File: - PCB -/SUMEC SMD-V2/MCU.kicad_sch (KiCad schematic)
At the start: 29 parts, among them IC2 DRV8874PWPR, IC3 DRV8874PWPR, J5 TYPE-C-31-M-12, SW2 SW_Push, SW3 SW_Push, U2 ESP32-S3-WROOM-1, U3 USBLC6-2SC6

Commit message: final fuckup cleanup
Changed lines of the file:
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@@
   )
   (text "0.1-µF bypass capacitor to ground, as well as\nsufficient Bulk Capacitance rated for VM"
-    (at 66.04 317.5 0)
+    (at 77.47 363.22 0)
     (effects (font (face "Bahnschrift") (size 1.27 1.27)) (justify left bottom))
   )
@@
   )
   (text "Sleep mode input. Logic high to enable device. \nLogic low to enter low-power sleep mode."
-    (at 66.04 312.42 0)
+    (at 77.47 358.14 0)
     (effects (font (face "Bahnschrift") (size 1.27 1.27)) (justify left bottom))
   )
@@
     (effects (font (face "Bahnschrift") (size 1.27 1.27)) (justify left bottom))
   )
-  (text "Overcurrent protection - Current regulation" (at 66.04 322.58 0)
+  (text "Overcurrent protection - Current regulation" (at 77.47 368.3 0)
     (effects (font (face "Bahnschrift") (size 1.27 1.27)) (justify left bottom))
   )
@@
   )
   (text "Analog current output propotaional to load current."
-    (at 66.04 320.04 0)
+    (at 77.47 365.76 0)
     (effects (font (face "Bahnschrift") (size 1.27 1.27)) (justify left bottom))
   )
@@
     (effects (font (face "Bahnschrift") (size 1.27 1.27)) (justify left bottom))
   )
-  (text "H-bridge control input mode." (at 66.04 307.34 0)
+  (text "H-bridge control input mode." (at 77.47 353.06 0)
     (effects (font (face "Bahnschrift") (size 1.27 1.27)) (justify left bottom))
   )
@@
   )
   (text "(nFault)Fault indicator output. Pulled low during a fault condition. \nConnect an external pullup resistor\nfor open-drain operation."
-    (at 66.04 302.26 0)
+    (at 77.47 347.98 0)
     (effects (font (face "Bahnschrift") (size 1.27 1.27)) (justify left bottom))
   )

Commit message: Board and BOM update
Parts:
- C16, C3, C5: footprint Capacitor_Tantalum_SMD:CP_EIA-2012-12_Kemet-R_Pad1.30x1.05mm_HandSolder -> Capacitor_Tantalum_SMD:CP_EIA-3216-18_Kemet-A_Pad1.58x1.35mm_HandSolder
- D3: footprint Diode_SMD:D_0805_2012Metric_Pad1.15x1.40mm_HandSolder -> Diode_SMD:D_1206_3216Metric_Pad1.42x1.75mm_HandSolder
- R4: footprint Resistor_SMD:R_0805_2012Metric_Pad1.20x1.40mm_HandSolder -> Resistor_SMD:R_1206_3216Metric_Pad1.30x1.75mm_HandSolder
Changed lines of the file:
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@@
       (effects (font (face "Bahnschrift") (size 1.27 1.27)))
     )
-    (property "Footprint" "Diode_SMD:D_0805_2012Metric_Pad1.15x1.40mm_HandSolder" (at 416.56 129.54 0)
+    (property "Footprint" "Diode_SMD:D_1206_3216Metric_Pad1.42x1.75mm_HandSolder" (at 416.56 129.54 0)
       (effects (font (face "Bahnschrift") (size 1.27 1.27)) hide)
     )
@@
       (effects (font (face "Bahnschrift") (size 1.27 1.27)))
     )
-    (property "Footprint" "Resistor_SMD:R_0805_2012Metric_Pad1.20x1.40mm_HandSolder" (at 417.83 145.542 90)
+    (property "Footprint" "Resistor_SMD:R_1206_3216Metric_Pad1.30x1.75mm_HandSolder" (at 417.83 145.542 90)
       (effects (font (face "Bahnschrift") (size 1.27 1.27)) hide)
     )
@@
       (effects (font (face "Bahnschrift") (size 1.27 1.27)) (justify left))
     )
-    (property "Footprint" "Capacitor_Tantalum_SMD:CP_EIA-2012-12_Kemet-R_Pad1.30x1.05mm_HandSolder" (at 233.9848 313.69 0)
+    (property "Footprint" "Capacitor_Tantalum_SMD:CP_EIA-3216-18_Kemet-A_Pad1.58x1.35mm_HandSolder" (at 233.9848 313.69 0)
       (effects (font (face "Bahnschrift") (size 1.27 1.27)) hide)
     )
@@
       (effects (font (face "Bahnschrift") (size 1.27 1.27)) (justify left))
     )
-    (property "Footprint" "Capacitor_Tantalum_SMD:CP_EIA-2012-12_Kemet-R_Pad1.30x1.05mm_HandSolder" (at 231.4448 356.87 0)
+    (property "Footprint" "Capacitor_Tantalum_SMD:CP_EIA-3216-18_Kemet-A_Pad1.58x1.35mm_HandSolder" (at 231.4448 356.87 0)
       (effects (font (face "Bahnschrift") (size 1.27 1.27)) hide)
     )
@@
       (effects (font (face "Bahnschrift") (size 1.27 1.27)) (justify left))
     )
-    (property "Footprint" "Capacitor_Tantalum_SMD:CP_EIA-2012-12_Kemet-R_Pad1.30x1.05mm_HandSolder" (at 209.8548 135.89 0)
-      (effects (font (face "Bahnschrift") (size 1.27 1.27)) hide)
-    )
+    (property "Footprint" "Capacitor_Tantalum_SMD:CP_EIA-3216-18_Kemet-A_Pad1.58x1.35mm_HandSolder" (at 209.8548 135.89 0)
+      (effects (font (face "Bahnschrift") (size 1.27 1.27)) hide)
+    )

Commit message: PCB Inspection
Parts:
- C19, C2: value 220nF.hb -> 100nF
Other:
- note added: "INPSECTED"
- note added: "PINOUT INPSECTED"
- note added: "TESTED - WORKS, INSPECTED"
- moved on the sheet: C1, C16, C17, C18, C19, C2, C3, C4, C5, C6, D1, D2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

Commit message: PCB update
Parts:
- R1, R2: value 220 -> 220R
- renumbered C3 to C1, C5 to C10, C7 to C11, C8 to C12, C9 to C13, C4 to C2, C18 to C3, C1 to C4, C19 to C5, C2 to C6, C17 to C7, C6 to C8, C16 to C9, IC2 to IC1, IC3 to IC2, J5 to J3, R4 to R5, R5 to R6, R6 to R7, R7 to R8, SW2 to SW3, SW3 to SW4, U2 to U1, U3 to U2
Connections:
- net POWER LED renamed LED2
- net TEST LED renamed LED1
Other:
- note added: "Status LED1"
- note added: "Status LED2"
- note removed: "Board power status"
- note removed: "Status LED"
- moved on the sheet: D1, D2, R1, R2

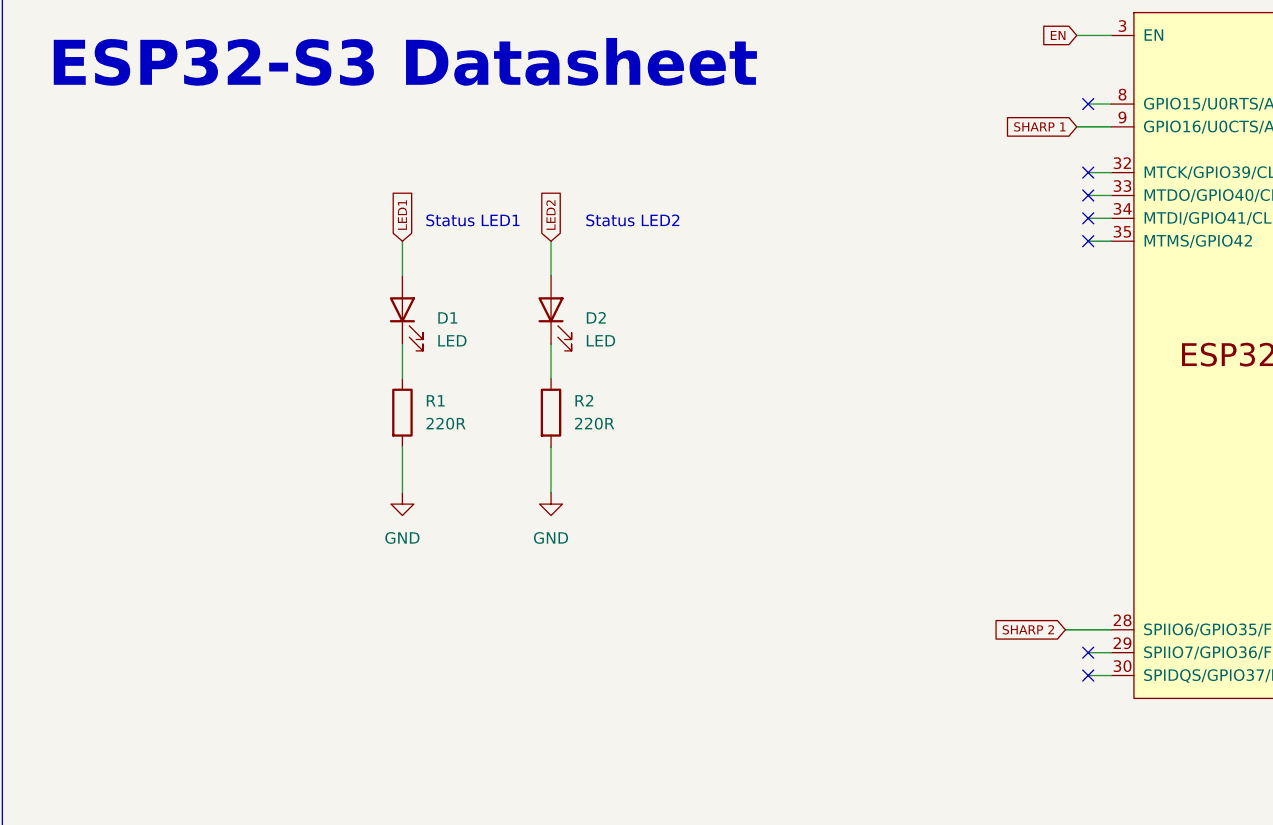
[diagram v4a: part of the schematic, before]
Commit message: PCB  Update, Buzzer, DRC.
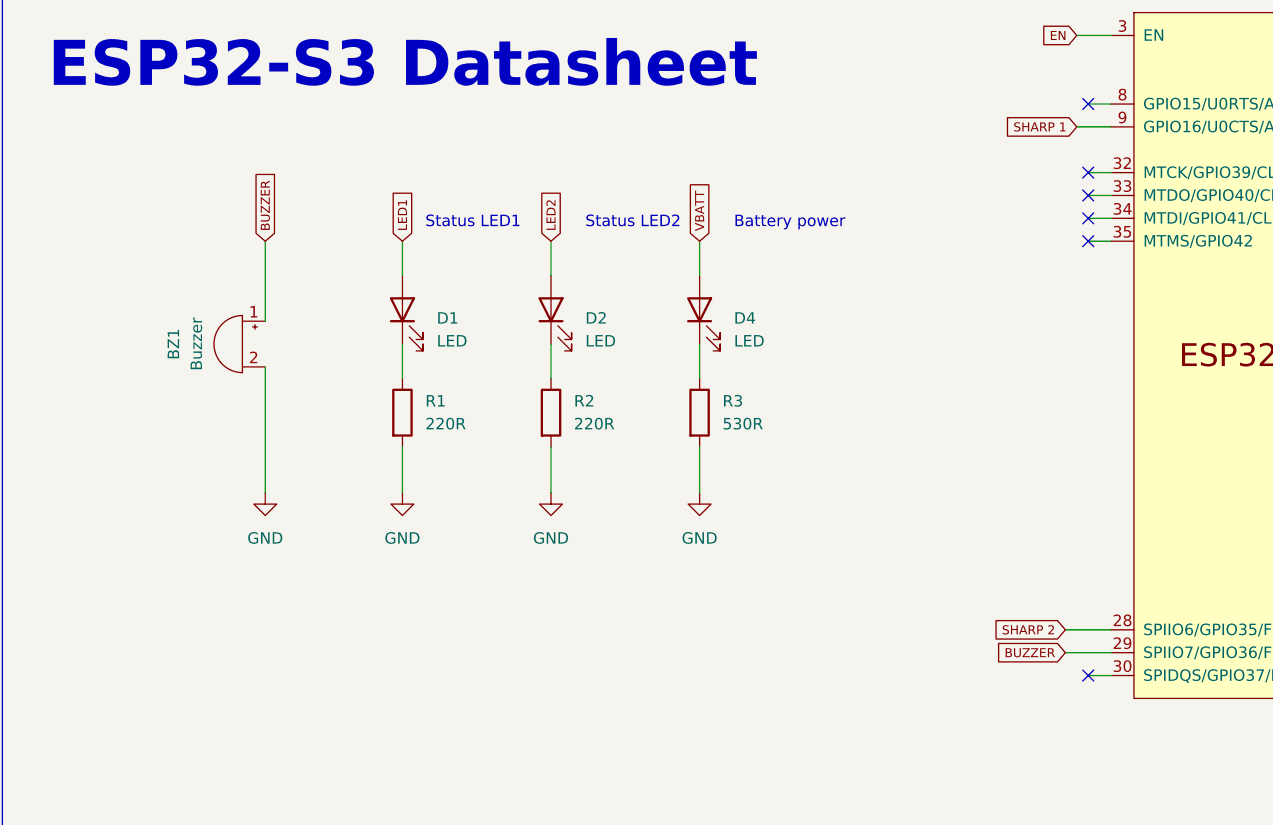
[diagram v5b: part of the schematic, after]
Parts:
- added BZ1: Buzzer, Buzzer_Beeper:MagneticBuzzer_CUI_CMT-8504-100-SMT, symbol Device:Buzzer
- added D4: LED, LED_SMD:LED_0805_2012Metric_Pad1.15x1.40mm_HandSolder, symbol Device:LED
- added R3: 530R, Resistor_SMD:R_0805_2012Metric_Pad1.20x1.40mm_HandSolder, symbol Device:R
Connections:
- net GND: now also BZ1.2 (+), R3.2
- net BUZZER: now reaches U1.29 (SPIIO7/GPIO36/FSPICLK/SUBSPICLK)
- net BUZZER: now also BZ1.1 (-)
- new net: D4.1 (K), R3.1
- new net VBATT: D4.2 (A)
- no-connect marks 29 -> 28
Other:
- note added: "Battery power"

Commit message: step update delete of buzzer
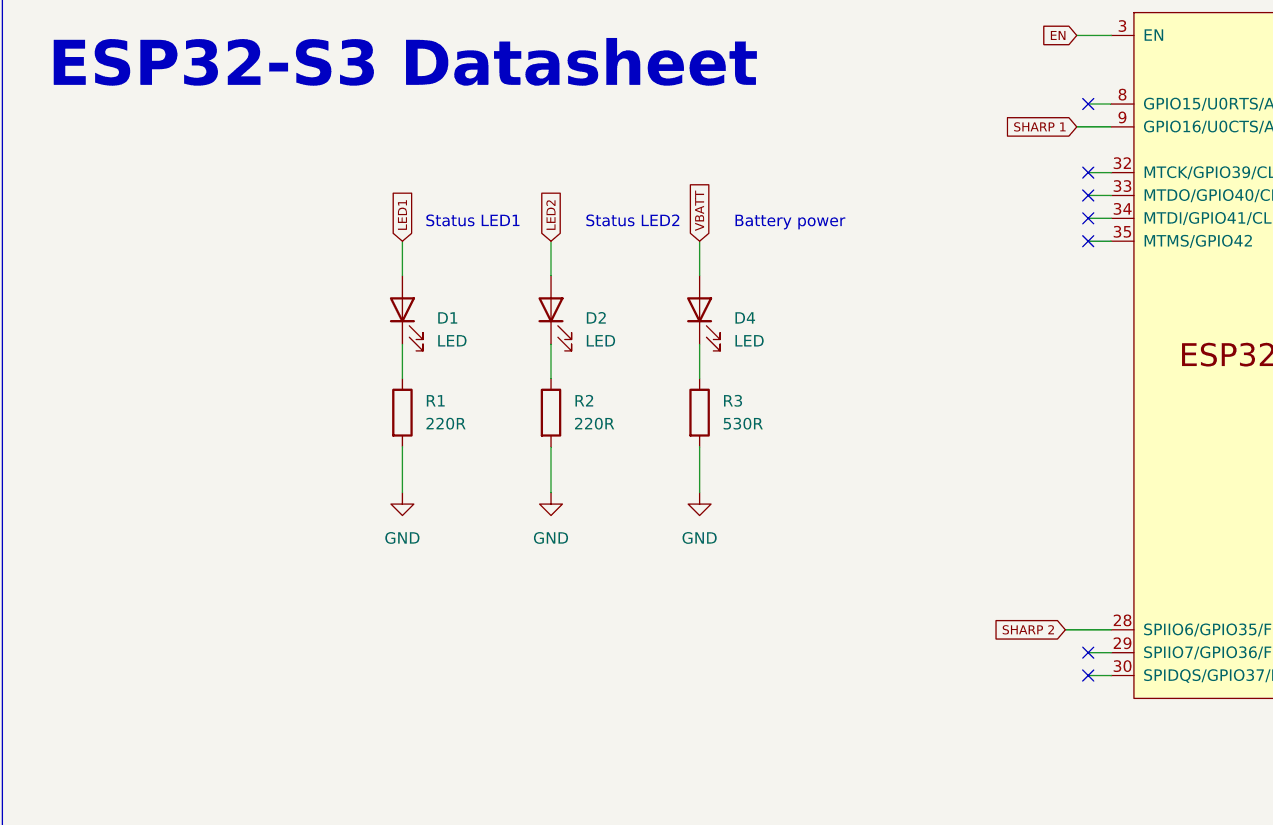
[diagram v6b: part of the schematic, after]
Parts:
- removed BZ1: Buzzer, Buzzer_Beeper:MagneticBuzzer_CUI_CMT-8504-100-SMT, symbol Device:Buzzer
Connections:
- net BUZZER: no longer names the net of U1.29 (SPIIO7/GPIO36/FSPICLK/SUBSPICLK)
- no-connect marks 28 -> 29
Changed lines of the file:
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@@
   (no_connect (at 162.56 190.5))
   (no_connect (at 457.2 134.62))
+  (no_connect (at 162.56 236.22))
   (no_connect (at 162.56 175.26))
   (no_connect (at 161.29 298.45))
@@
     (stroke (width 0) (type default))
   )
-  (wire (pts (xy 71.12 204.47) (xy 71.12 218.44))
-    (stroke (width 0) (type default))
-  )
   (wire (pts (xy 218.44 346.71) (xy 229.87 346.71))
     (stroke (width 0) (type default))
@@
     (stroke (width 0) (type default))
   )
-  (wire (pts (xy 160.02 236.22) (xy 165.1 236.22))
+  (wire (pts (xy 162.56 236.22) (xy 165.1 236.22))
     (stroke (width 0) (type default))
   )
@@
   )
   (wire (pts (xy 458.47 137.16) (xy 457.2 137.16))
-    (stroke (width 0) (type default))
-  )
-  (wire (pts (xy 71.12 199.39) (xy 71.12 190.5))
     (stroke (width 0) (type default))
   )
@@
     )
   )
-  (global_label "BUZZER" (shape input) (at 160.02 236.22 180) (fields_autoplaced)
-    (effects (font (face "Bahnschrift") (size 1 1) (color 0 0 0 1)) (justify right))
-    (property "Intersheetrefs" "${INTERSHEET_REFS}" (at 152.8417 236.22 0)
-      (effects (font (size 1.27 1.27)) (justify right) hide)
-    )
-  )
   (global_label "VBATT" (shape input) (at 119.38 190.5 90) (fields_autoplaced)
     (effects (font (face "Bahnschrift") (size 1 1) (color 0 0 0 1)) (justify left))
@@
     (effects (font (face "Bahnschrift") (size 1 1) (color 0 0 0 1)) (justify left))
     (property "Intersheetrefs" "${INTERSHEET_REFS}" (at 526.8764 139.7 0)
-      (effects (font (size 1.27 1.27)) (justify left) hide)
-    )
-  )
-  (global_label "BUZZER" (shape input) (at 71.12 190.5 90) (fields_autoplaced)
-    (effects (font (face "Bahnschrift") (size 1 1) (color 0 0 0 1)) (justify left))
-    (property "Intersheetrefs" "${INTERSHEET_REFS}" (at 71.12 183.3217 90)
       (effects (font (size 1.27 1.27)) (justify left) hide)
     )
@@
         (path "/fc70a1a8-ed7c-4a0f-9b1a-f23293528385/11aa20d4-c4ff-49be-9179-c2911da50f67"
           (reference "#PWR018") (unit 1)
-        )
-      )
-    )
-  )
-  (symbol (lib_id "power:GND") (at 71.12 218.44 0) (unit 1)
-    (in_bom yes) (on_board yes) (dnp no) (fields_autoplaced)
-    (property "Reference" "#PWR050" (at 71.12 224.79 0)
-      (effects (font (face "Bahnschrift") (size 1.27 1.27)) hide)
-    )
-    (property "Value" "GND" (at 71.12 223.52 0)
-      (effects (font (face "Bahnschrift") (size 1.27 1.27)))
-    )
-    (property "Footprint" "" (at 71.12 218.44 0)
-      (effects (font (face "Bahnschrift") (size 1.27 1.27)) hide)
-    )
-    (property "Datasheet" "" (at 71.12 218.44 0)
-      (effects (font (face "Bahnschrift") (size 1.27 1.27)) hide)
-    )
-    (pin "1")
-    (instances
-      (project "sumec"
-        (path "/fc70a1a8-ed7c-4a0f-9b1a-f23293528385/11aa20d4-c4ff-49be-9179-c2911da50f67"
-          (reference "#PWR050") (unit 1)
         )
       )
@@
         )
       )
-    )
-  )
-  (symbol (lib_id "Device:Buzzer") (at 68.58 201.93 0) (mirror y) (unit 1)
-    (in_bom yes) (on_board yes) (dnp no)
-    (property "Reference" "BZ1" (at 60.96 201.93 90)
-      (effects (font (face "Bahnschrift") (size 1.27 1.27)))
-    )
-    (property "Value" "Buzzer" (at 63.5 201.93 90)
-      (effects (font (face "Bahnschrift") (size 1.27 1.27)))
-    )
-    (property "Footprint" "Buzzer_Beeper:MagneticBuzzer_CUI_CMT-8504-100-SMT" (at 69.215 199.39 90)
-      (effects (font (face "Bahnschrift") (size 1.27 1.27)) hide)
-    )
-    (property "Datasheet" "~" (at 69.215 199.39 90)
-      (effects (font (face "Bahnschrift") (size 1.27 1.27)) hide)
-    )
-    (pin "1")
-    (pin "2")
-    (instances
-      (project "sumec"
-        (path "/fc70a1a8-ed7c-4a0f-9b1a-f23293528385"
-          (reference "BZ1") (unit 1)
-        )
-        (path "/fc70a1a8-ed7c-4a0f-9b1a-f23293528385/11aa20d4-c4ff-49be-9179-c2911da50f67"
-          (reference "BZ1") (unit 1)
-        )
-      )

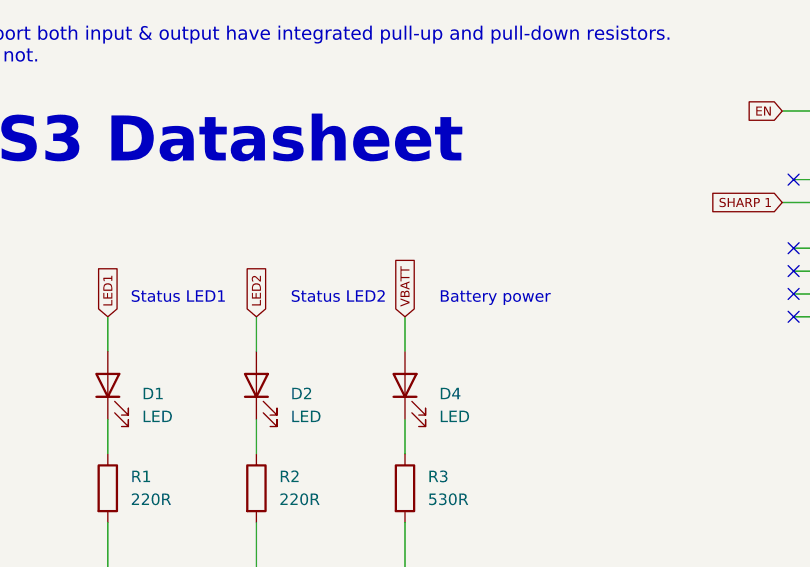
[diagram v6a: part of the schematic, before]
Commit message: LED 12V change
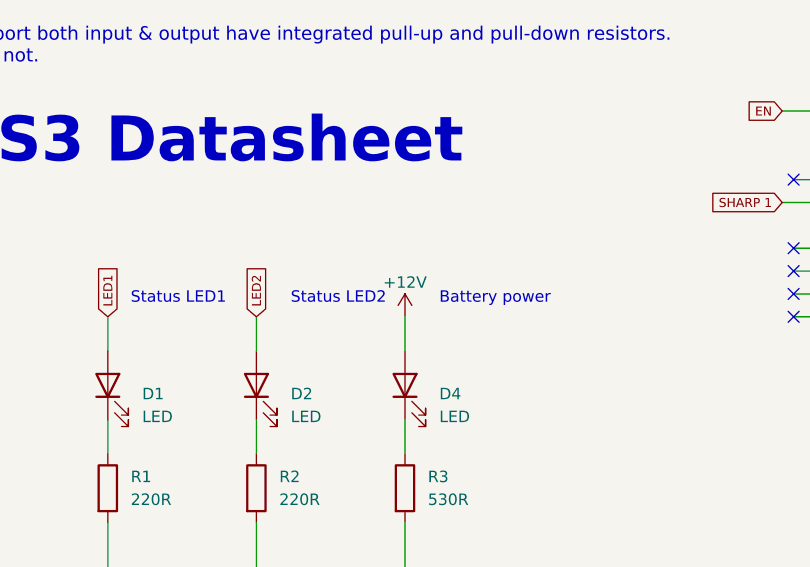
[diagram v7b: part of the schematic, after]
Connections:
- net VBATT is gone; now on net +12V: D4.2 (A)
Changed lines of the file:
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@@
-    )
-  )
-  (global_label "VBATT" (shape input) (at 119.38 190.5 90) (fields_autoplaced)
-    (effects (font (face "Bahnschrift") (size 1 1) (color 0 0 0 1)) (justify left))
-    (property "Intersheetrefs" "${INTERSHEET_REFS}" (at 119.38 184.284 90)
-      (effects (font (size 1.27 1.27)) (justify left) hide)
     )
   )
@@
         )
       )
+    )
+  )
+  (symbol (lib_id "power:+12V") (at 119.38 190.5 0) (mirror y) (unit 1)
+    (in_bom yes) (on_board yes) (dnp no) (fields_autoplaced)
+    (property "Reference" "#PWR050" (at 119.38 194.31 0)
+      (effects (font (face "Bahnschrift") (size 1.27 1.27)) hide)
+    )
+    (property "Value" "+12V" (at 119.38 186.69 0)
+      (effects (font (face "Bahnschrift") (size 1.27 1.27)))
+    )
+    (property "Footprint" "" (at 119.38 190.5 0)
+      (effects (font (face "Bahnschrift") (size 1.27 1.27)) hide)
+    )
+    (property "Datasheet" "" (at 119.38 190.5 0)
+      (effects (font (face "Bahnschrift") (size 1.27 1.27)) hide)
+    )
+    (pin "1")
+    (instances
+      (project "sumec"
+        (path "/fc70a1a8-ed7c-4a0f-9b1a-f23293528385/11aa20d4-c4ff-49be-9179-c2911da50f67"
+          (reference "#PWR050") (unit 1)
+        )
+      )

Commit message: BOM update
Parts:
- R1, R2: value 220R -> 100R
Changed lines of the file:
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@@
       (effects (font (face "Bahnschrift") (size 1.27 1.27)) (justify left))
     )
-    (property "Value" "220R" (at 88.9 210.82 0)
+    (property "Value" "100R" (at 88.9 210.82 0)
       (effects (font (face "Bahnschrift") (size 1.27 1.27)) (justify left))
     )
@@
       (effects (font (face "Bahnschrift") (size 1.27 1.27)) (justify left))
     )
-    (property "Value" "220R" (at 105.41 210.82 0)
-      (effects (font (face "Bahnschrift") (size 1.27 1.27)) (justify left))
-    )
+    (property "Value" "100R" (at 105.41 210.82 0)
+      (effects (font (face "Bahnschrift") (size 1.27 1.27)) (justify left))
+    )
